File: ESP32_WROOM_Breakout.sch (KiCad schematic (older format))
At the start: 16 parts

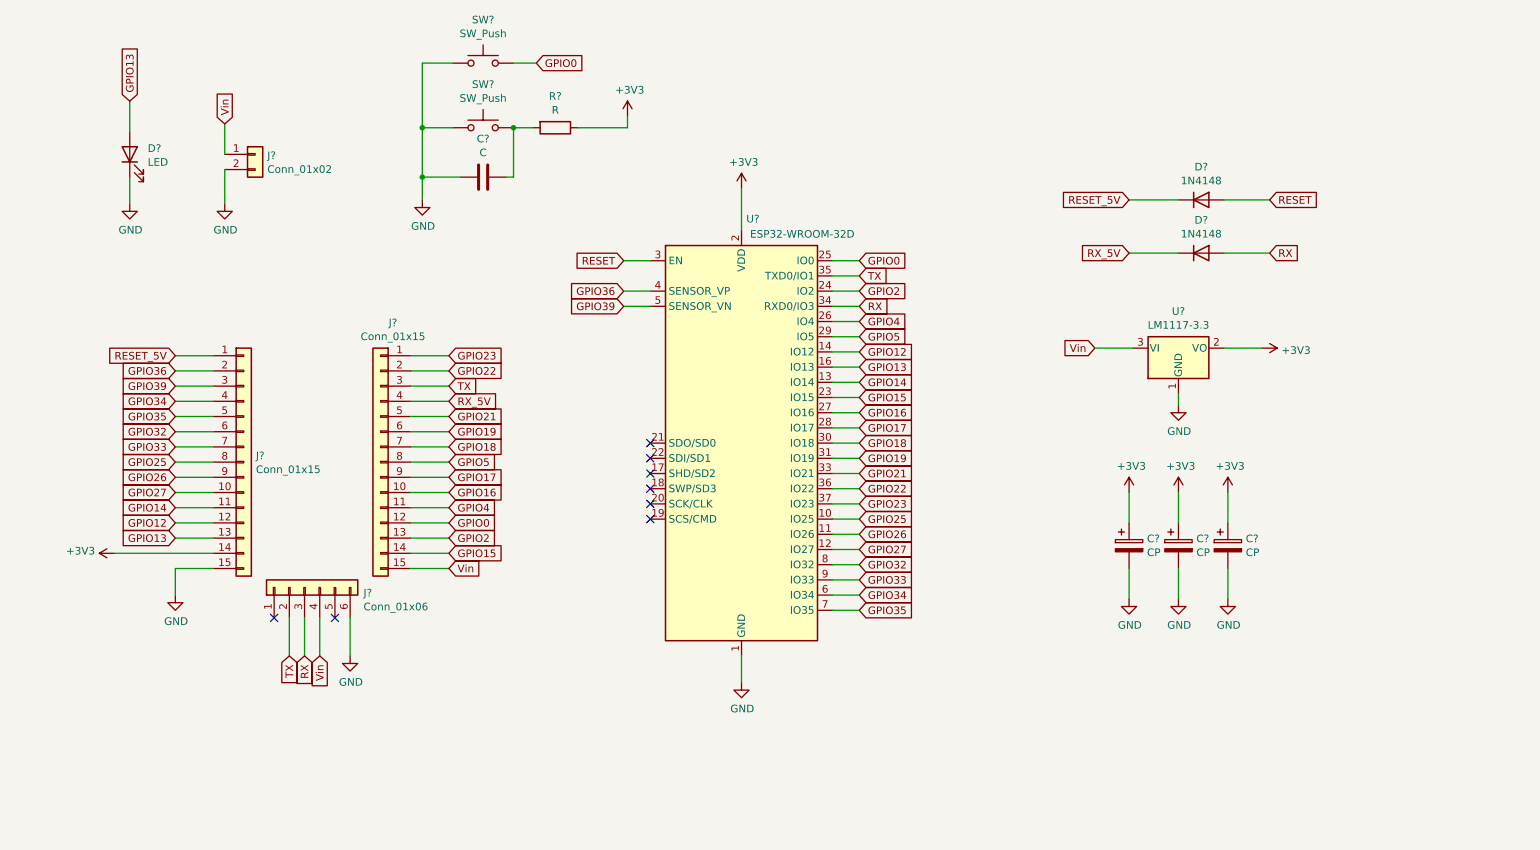
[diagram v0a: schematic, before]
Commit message: sch documented
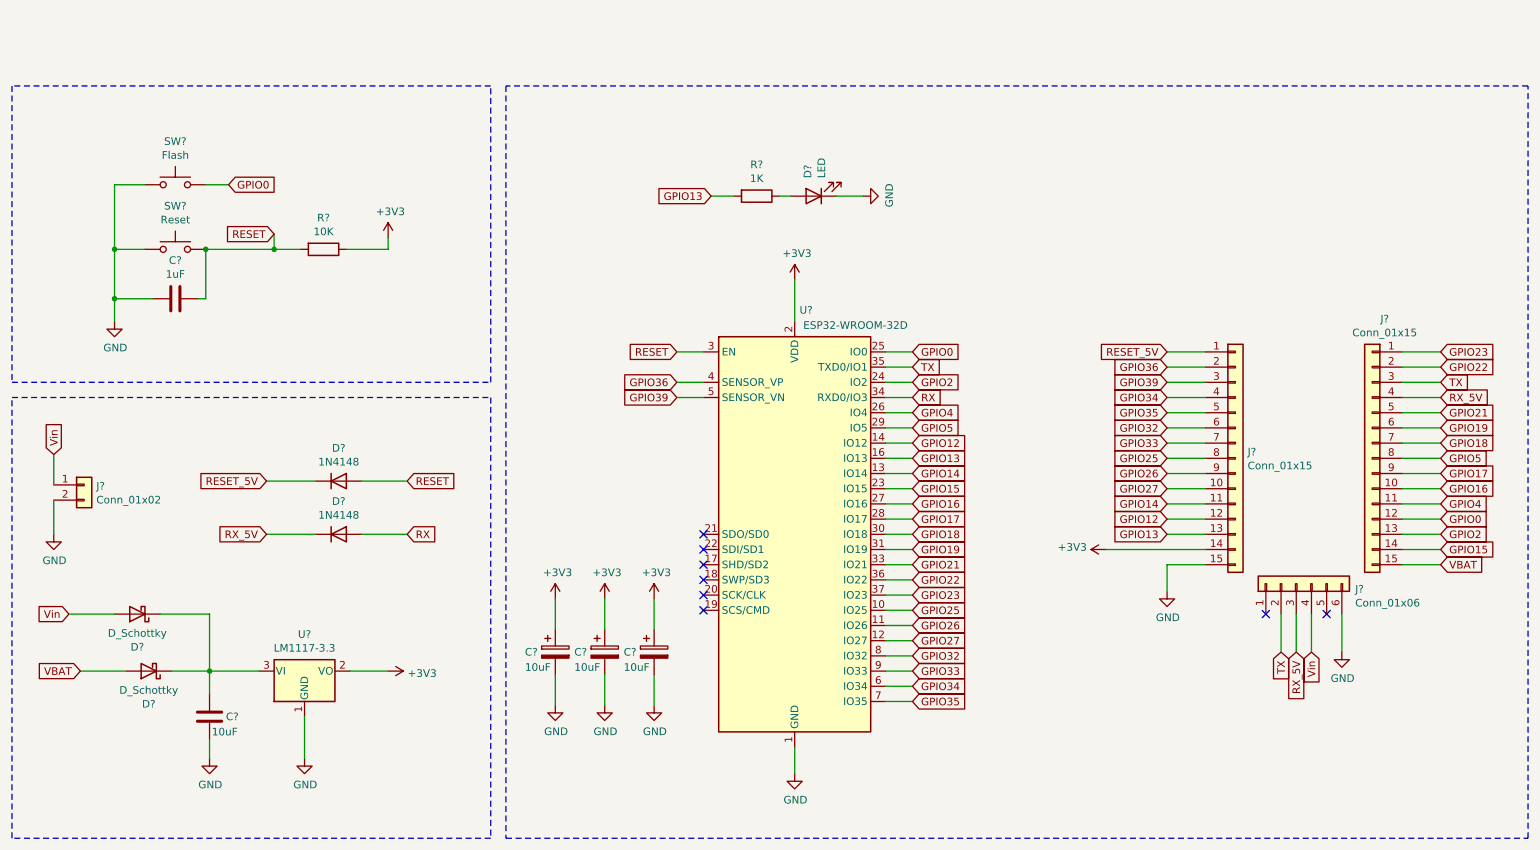
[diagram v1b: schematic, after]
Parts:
- added C?: 10uF, symbol Device:C
- added D? (x2): D_Schottky, symbol Device:D_Schottky
- added R?: 1K, symbol Device:R
- C? (x3): value CP -> 10uF
- C?: value C -> 1uF
- R?: value R -> 10K
- SW?: value SW_Push -> Flash
- SW?: value SW_Push -> Reset
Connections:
- net GND: now also C?.1
- net GPIO13: now also R?.2; no longer D?.2 (A)
- net RESET: now also C?.1, R?.2, SW?.2
- net RX: no longer J?.3 (Pin_3)
- net RX_5V: now also J?.3 (Pin_3)
- net Vin: now also D?.2 (A); no longer J?.15 (Pin_15), U?.3 (VI)
- new net: C?.2, D?.1 (K), D?.1 (K), U?.3 (VI)
- new net: D?.2 (A), R?.1
- new net VBAT: D?.2 (A), J?.15 (Pin_15)
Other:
- moved on the sheet: C?, D?, J?, R?, SW?, U?
